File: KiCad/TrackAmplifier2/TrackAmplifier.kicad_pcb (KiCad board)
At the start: 2 copper layers, 105 x 70 mm, 109 parts, among them J1 DB15_Male_MountingHoles, J2 Conn_01x06, Q1 2N7002, U1 ST485EBDR, U10 REF3025, U11 LM35-LP, U2 ST485EBDR, U3 LM78M05_TO252, U4 LMD18200, U5 ST485EBDR, U6 ST485EBDR, U7 INA326, U8 INA326, U9 PIC16F18854-SO

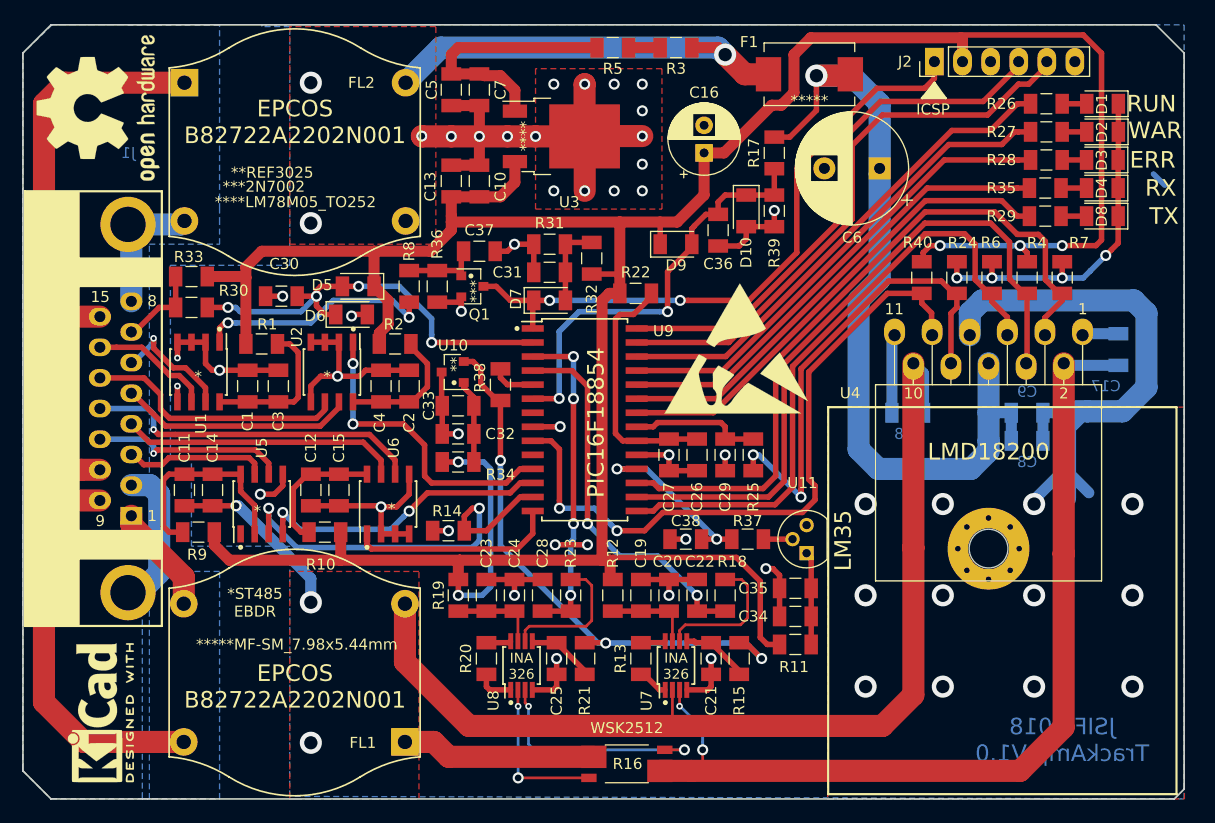
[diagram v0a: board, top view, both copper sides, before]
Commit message: updated schematic and layout, not finished yet. To do: - Update components with real used values
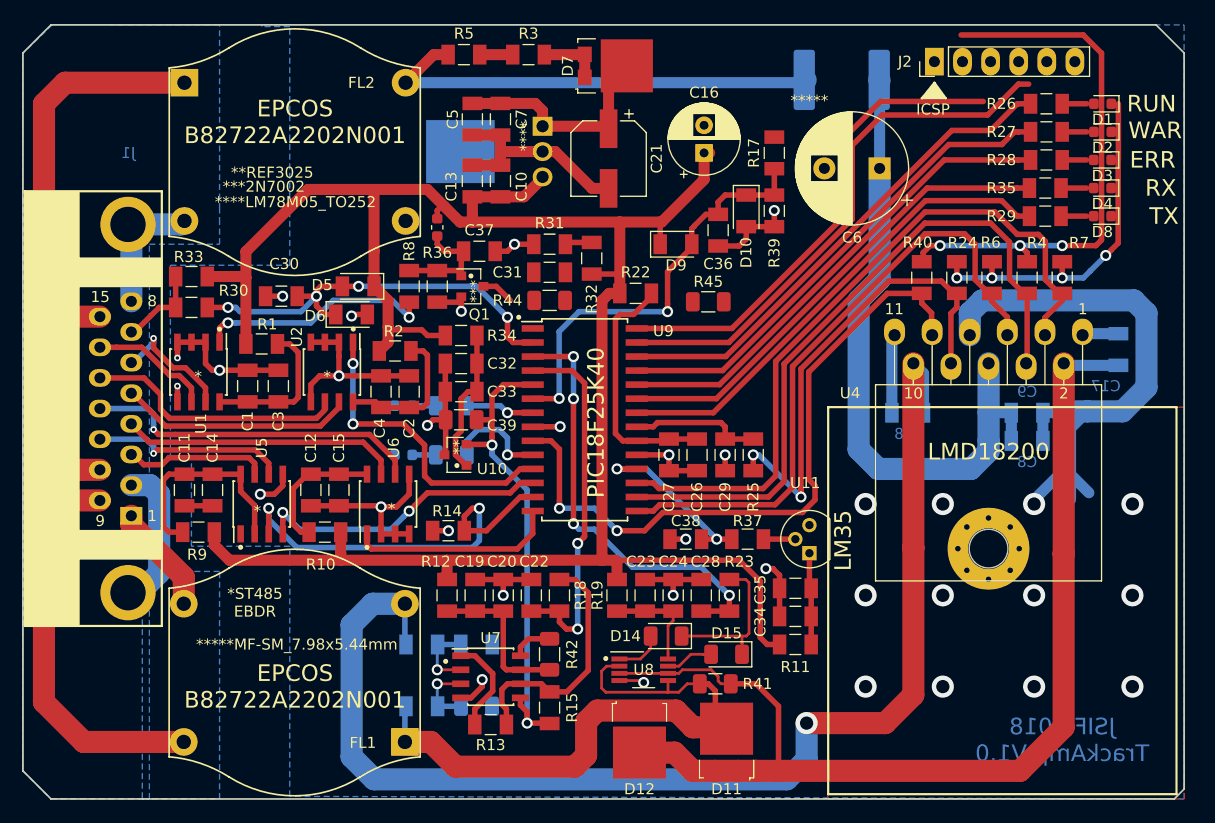
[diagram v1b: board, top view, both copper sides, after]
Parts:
- removed C25: 100n, Capacitor_SMD:C_1206_3216Metric
- removed REF**: ESD-Logo_13.2x12mm_SilkScreen, Symbol:ESD-Logo_13.2x12mm_SilkScreen
- removed REF**: KiCad-Logo2_6mm_SilkScreen, Symbol:KiCad-Logo2_6mm_SilkScreen
- removed REF**: OSHW-Logo2_14.6x12mm_SilkScreen, Symbol:OSHW-Logo2_14.6x12mm_SilkScreen
- added C39: 4.7u, Capacitor_SMD:C_1206_3216Metric, F.Cu at (89.6, 85.7)
- added D11: VS-6ESH06-M3, Package_TO_SOT_SMD:TO-277A, F.Cu at (113.6, 114.7)
- added D12: VS-6ESH06-M3, Package_TO_SOT_SMD:TO-277A, F.Cu at (105.8, 114.8)
- added D13: LED BL ?, LED_SMD:LED_0603_1608Metric, B.Cu at (84.4, 88.9)
- added D14: 1n4148, Diode_SMD:D_1206_3216Metric, F.Cu at (108.2, 105.3)
- added D15: 1n4148, Diode_SMD:D_1206_3216Metric, F.Cu at (113.6, 106.9)
- added D16: LED BL, LED_SMD:LED_0603_1608Metric, B.Cu at (84.4, 84.4)
- added R41: 47E, Resistor_SMD:R_1206_3216Metric, F.Cu at (112.6, 109.6)
- added R42: 4k7, Resistor_SMD:R_1206_3216Metric, F.Cu at (97.6, 106.9)
- added R43: 300E, Resistor_SMD:R_1206_3216Metric, B.Cu at (88.7, 88.9)
- added R44: 470, Resistor_SMD:R_1206_3216Metric, F.Cu at (97.6, 74.9)
- added R45: 470, Resistor_SMD:R_1206_3216Metric, F.Cu at (112.0, 75.0)
- added R46: 300E, Resistor_SMD:R_1206_3216Metric, B.Cu at (88.7, 84.4)
- added R47: NP, Resistor_SMD:R_0603_1608Metric, F.Cu at (87.5, 68.3)
- C1, C11, C12, C13, C19, C2, C23, C26, C32, C34, C38, C5, C8: value 22u -> 4.7u
- C16: value 100u -> 220u
- C21: value 100n -> 470u; footprint Capacitor_SMD:C_1206_3216Metric -> Capacitor_SMD:CP_Elec_6.3x3
- C22, C28: value 1u -> 100n
- C29: value 22u -> 100n
- C30: value 220n -> 100n
- C36: value 220n -> 4.7u
- D1, D4, D8: value LED -> LED GR; footprint LED_SMD:LED_1206_3216Metric -> LED_SMD:LED_0603_1608Metric
- D2: value LED -> LED YE; footprint LED_SMD:LED_1206_3216Metric -> LED_SMD:LED_0603_1608Metric
- D3: value LED -> LED RD; footprint LED_SMD:LED_1206_3216Metric -> LED_SMD:LED_0603_1608Metric
- D7: value 1n4148 -> VS-6ESH06-M3; footprint Diode_SMD:D_1206_3216Metric -> Package_TO_SOT_SMD:TO-277A
- F1: value 3.0A -> 2.5A; footprint Fuse:Fuse_Bourns_MF-SM_7.98x5.44mm -> Fuse:Fuse_2920_7451Metric; moved to B.Cu
- Q1: value 2N7002 -> NTR5103NT1G
- R1, R10, R11, R2, R22, R9: value 10E -> 0E
- R13: value 10E -> 1k
- R14: value 4K7 -> 1k
- R15: value 10E -> 110k
- R16: value 0.025 -> 1k; footprint Resistor_SMD:R_Shunt_2512_6332Metric_0.005-0.2 -> Resistor_SMD:R_1206_3216Metric; moved to B.Cu
- R17: value 10k -> 5k1
- R20, R21: value 10E -> 9k10; moved to B.Cu
- R25: value 1K -> 4k7
- R26, R27, R28, R29, R35: value 330E -> 300E
- R30: value 10k -> 1k
- R31: value 100K -> 110k
- R33: value 1K -> 470
- R38: value 10E -> 1k; moved to B.Cu
- R39: value 50k -> 910R
- R4, R6, R7: value 4K7 -> 4k7
- R8: value 100E -> 1k
- U10: value REF3025 -> MCP1525
- U11: value LM35-LP -> MCP9701A-E/TO
- U3: value LM78M05_TO252 -> L78M05CDT-1-TO-251-3; footprint Package_TO_SOT_SMD:TO-252-2 -> Package_TO_SOT_THT:TO-251-3-1EP_Horizontal_TabDown; moved to B.Cu
- U7: value INA326 -> MCP6N11; footprint Package_SO:MSOP-8_3x3mm_P0.65mm -> Package_SO:SOIC-8_3.9x4.9mm_P1.27mm
- U8: value INA326 -> INA2180; footprint Package_SO:MSOP-8_3x3mm_P0.65mm -> Package_SO:VSSOP-8_3.0x3.0mm_P0.65mm
- U9: value PIC16F18854-SO -> PIC18F25K40
- moved C21 46.2 mm to (103.0, 62.1), turned to 270 degrees
- moved R38 23.6 mm to (91.0, 106.0), turned to 0 degrees
- moved D7 22.0 mm to (103.6, 53.7), turned to 90 degrees
- moved R15 17.7 mm to (97.6, 111.7)
- moved U7 16.8 mm to (92.3, 109.0), turned to 0 degrees
- moved C20 15.0 mm to (93.4, 101.6)
- moved R12 15.0 mm to (88.4, 101.6)
- moved R18 15.0 mm to (98.5, 101.6)
- moved C19 15.0 mm to (90.9, 101.6)
- moved C22 15.0 mm to (96.0, 101.6)
- moved R13 14.8 mm to (92.3, 113.3), turned to 180 degrees
- moved R21 14.8 mm to (86.1, 106.0), turned to 0 degrees
- moved R16 14.6 mm to (91.0, 111.6), turned to 0 degrees
- moved C23 14.4 mm to (106.3, 101.6)
- moved C24 14.4 mm to (108.8, 101.6)
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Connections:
- C17 pad 2: PWM1 -> OCC1
- C21 pad 1: GND -> Net-(C21-Pad1)
- C21 pad 2: Net-(C21-Pad2) -> GND
- C5 pad 2: +15V -> Net-(C21-Pad1)
- C7 pad 2: +15V -> Net-(C21-Pad1)
- D7 pad 1: RST -> Net-(D7-Pad1)
- D7 pad 2: Net-(C31-Pad2) -> Net-(D7-Pad1)
- FL1 pad 1: Net-(FL1-Pad1) -> OCC2
- J2 pad 1: RST -> VPP
- R15 pad 1: VREF -> Net-(R13-Pad1)
- R15 pad 2: Net-(C21-Pad2) -> VREF
- R16 pad 1: PWM1 -> Net-(R16-Pad1)
- R16 pad 2: OCC1 -> GND
- R18 pad 2: Net-(R18-Pad2) -> Net-(R13-Pad1)
- R20 pad 1: Net-(R20-Pad1) -> Net-(R16-Pad1)
- R20 pad 2: Net-(R20-Pad2) -> OCC2
- R21 pad 1: VREF -> PWM2
- R21 pad 2: Net-(C25-Pad2) -> Net-(R21-Pad2)
- R23 pad 2: Net-(R23-Pad2) -> Net-(D14-Pad1)
- R3 pad 1: Vbus_flt -> Net-(R3-Pad1)
- R3 pad 2: Net-(R3-Pad2) -> Net-(D7-Pad1)
- R38 pad 1: VREF -> Net-(R21-Pad2)
- R38 pad 2: Net-(R38-Pad2) -> GND
- R5 pad 1: Net-(R3-Pad2) -> Vbus_flt
- R5 pad 2: +15V -> Net-(R3-Pad1)
- U3 pad 1: +15V -> Net-(C21-Pad1)
- U4 pad 2: PWM1 -> OCC1
- U7 pad 1: Net-(R13-Pad1) -> Net-(R13-Pad2)
- U7 pad 2: PWM2 -> Net-(R21-Pad2)
- U7 pad 3: PWM1 -> Net-(R16-Pad1)
- U7 pad 5: Net-(C21-Pad2) -> VREF
- U7 pad 6: Net-(R18-Pad2) -> Net-(R13-Pad1)
- U7 pad 8: Net-(R13-Pad2) -> Net-(R42-Pad2)
- U8 pad 1: Net-(R20-Pad1) -> Net-(D14-Pad2)
- U8 pad 5: Net-(C25-Pad2) -> OCC2
- U8 pad 6: Net-(R23-Pad2) -> OCC1
- U8 pad 7: Net-(C23-Pad2) -> Net-(D15-Pad2)
- U8 pad 8: Net-(R20-Pad2) -> Net-(C23-Pad2)
- U9 pad 5: Net-(R38-Pad2) -> VREF
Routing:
- net PWM1: track 85.3 -> 0.00 mm, vias 2 -> 0
- net OCC1: track 21.1 -> 100.5 mm, vias 2 -> 0
- net RST: track 58.2 -> 2.96 mm, vias 2 -> 0
- net GND: track 270.0 -> 226.7 mm, vias 61 -> 38
- net OCC2: track 14.3 -> 57.6 mm, vias 2 -> 0
- net +5V: track 283.0 -> 244.8 mm, vias 5 -> 3
- net +15V: track 23.4 -> 0.00 mm
- net Net-(C21-Pad1): track 0.00 -> 20.5 mm
- net PWM2: track 92.9 -> 112.9 mm, vias 0 -> 1
- net Net-(R13-Pad1): track 2.76 -> 22.6 mm
- net Net-(FL1-Pad1): track 17.6 -> 0.00 mm
- net Net-(C6-Pad1): track 77.4 -> 61.3 mm, vias 1 -> 0
- net Net-(D14-Pad1): track 0.00 -> 14.3 mm
- net Net-(R18-Pad2): track 12.8 -> 0.00 mm
- net Net-(R23-Pad2): track 12.7 -> 0.00 mm
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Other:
- board text added: "PIC18F25K40"
- board text removed: "INA 326"
- board text removed: "PIC16F18854"
- board text removed: "WSK2512"

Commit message: Updated schematic according to proto board.
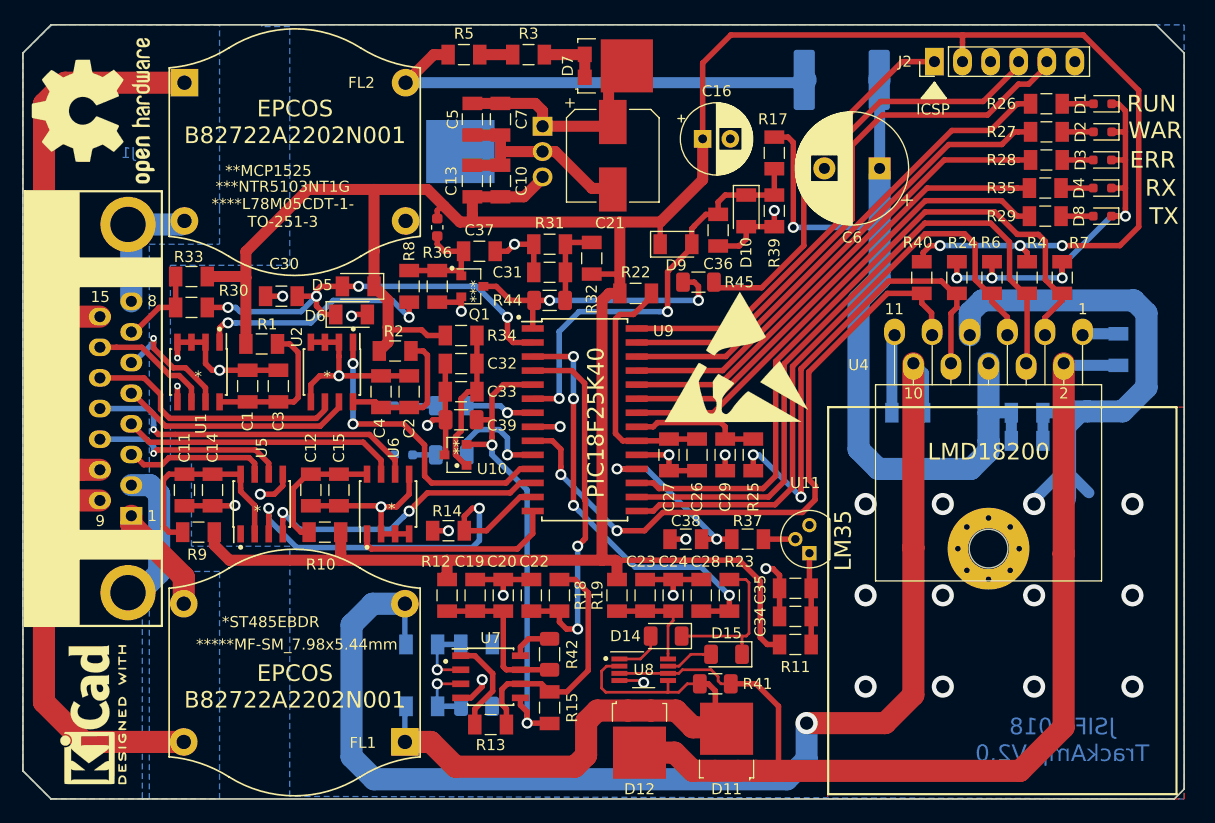
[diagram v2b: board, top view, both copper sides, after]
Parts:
- added REF**: ESD-Logo_13.2x12mm_SilkScreen, Symbol:ESD-Logo_13.2x12mm_SilkScreen, F.Cu at (114.5, 80.0)
- added REF**: OSHW-Logo2_14.6x12mm_SilkScreen, Symbol:OSHW-Logo2_14.6x12mm_SilkScreen, F.Cu at (56.4, 57.8)
- added REF**: KiCad-Logo2_6mm_SilkScreen, Symbol:KiCad-Logo2_6mm_SilkScreen, F.Cu at (56.4, 112.4)
- C21: footprint Capacitor_SMD:CP_Elec_6.3x3 -> Capacitor_SMD:CP_Elec_8x10.5
- D1, D13, D16, D2, D3, D4, D8: footprint LED_SMD:LED_0603_1608Metric -> Diode_SMD:LED_0.8x0.8
- moved R45 1.99 mm to (111.1, 73.3)
- moved C16 1.28 mm to (111.5, 60.3), turned to 0 degrees
- moved C21 0.46 mm to (103.3, 61.8)
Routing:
- net +5V: track 244.8 -> 283.2 mm
- net VPP: track 0.00 -> 32.9 mm
- net RST: track 2.96 -> 25.4 mm, vias 0 -> 2
- net Net-(C6-Pad1): track 61.3 -> 78.7 mm, vias 0 -> 1
- net GND: track 226.7 -> 237.0 mm, vias 38 -> 39
- net Net-(C31-Pad2): track 2.45 -> 7.54 mm
- net ICSPDAT: track 44.0 -> 48.9 mm
- net ICSPCLK: track 49.0 -> 51.7 mm
- net THFLG: track 62.3 -> 60.5 mm
- net OCC: track 39.5 -> 38.6 mm
- net Net-(D2-Pad2): track 2.22 -> 2.83 mm
- net Net-(D1-Pad2): track 2.22 -> 2.83 mm
- net Net-(D8-Pad2): track 2.30 -> 2.91 mm
- net Net-(D4-Pad2): track 2.30 -> 2.91 mm
- net Net-(D3-Pad2): track 2.20 -> 2.81 mm
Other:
- board text added: "****L78M05CDT-1- TO-251-3"
- board text added: "***NTR5103NT1G"
- board text added: "**MCP1525"
- board text added: "*ST485EBDR"
- board text added: "JSIF 2018 TrackAmp V2.0"
- board text added: "OCCUPIED"
- board text removed: "****LM78M05_TO252"
- board text removed: "***2N7002"
- board text removed: "**REF3025"
- board text removed: "*ST485 EBDR"
- board text removed: "C17"
- board text removed: "C18"
- board text removed: "C8"
- board text removed: "C9"
- board text removed: "JSIF 2018 TrackAmp V1.0"

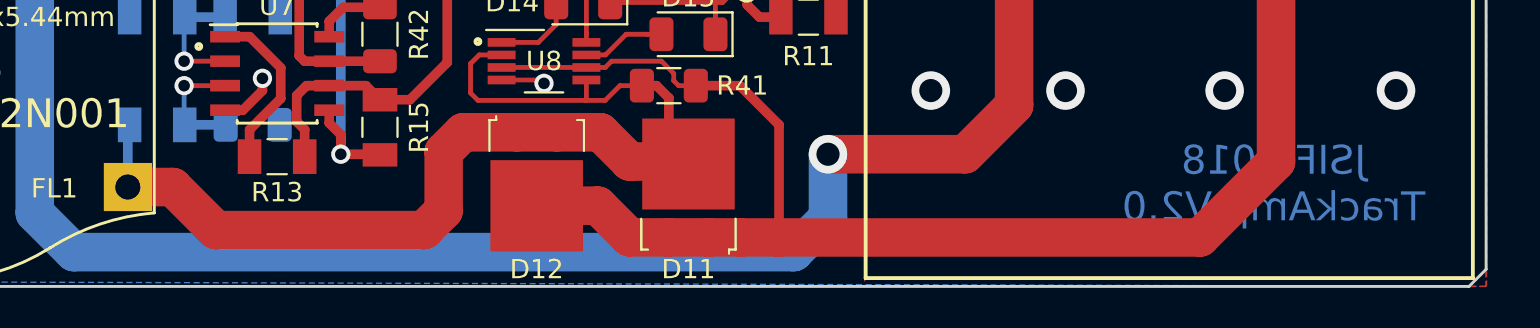
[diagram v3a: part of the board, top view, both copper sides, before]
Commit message: updated year notifications to 2019
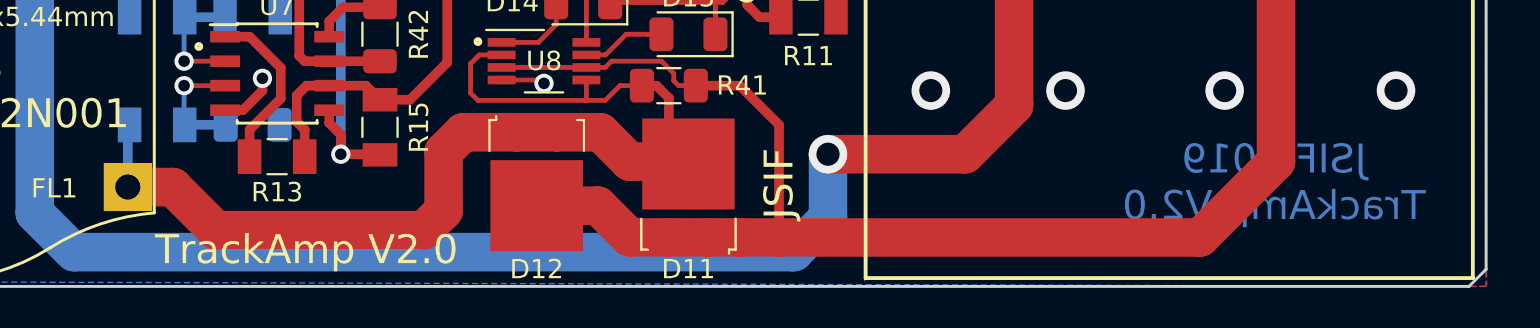
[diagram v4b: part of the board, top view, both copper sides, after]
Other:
- board text added: "JSIF"
- board text added: "JSIF 2019 TrackAmp V2.0"
- board text added: "TrackAmp V2.0"
- board text removed: "JSIF 2018 TrackAmp V2.0"
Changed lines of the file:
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@@
   (general
     (thickness 1.6)
-    (drawings 85)
+    (drawings 87)
     (tracks 918)
     (zones 0)
@@
     )
   )
+  (gr_text JSIF (at 118.326 114.666 90) (layer F.SilkS)
+    (effects (font (size 1.5 1.5) (thickness 0.3)))
+  )
+  (gr_text "TrackAmp V2.0" (at 93.815 118.095) (layer F.SilkS)
+    (effects (font (size 1.5 1.5) (thickness 0.3)))
+  )
   (gr_text 8 (at 61.684 74.9785) (layer B.SilkS)
     (effects (font (size 1 1) (thickness 0.15)) (justify mirror))
@@
     (effects (font (size 1.5 1.5) (thickness 0.3)) (justify mirror))
   )
-  (gr_text "JSIF 2018 \nTrackAmp V2.0" (at 143.98 114.666) (layer B.SilkS)
+  (gr_text "JSIF 2019 \nTrackAmp V2.0" (at 144 114.6) (layer B.SilkS)
     (effects (font (size 1.5 1.5) (thickness 0.3)) (justify mirror))
   )
@@
   (gr_line (start 132.423 55.357) (end 131.534 56.5) (layer F.SilkS) (width 0.2))
   (gr_line (start 133.185 56.5) (end 132.423 55.357) (layer F.SilkS) (width 0.2))
-  (gr_text "JSIF 2018 \nTrackAmp V2.0" (at 143.98 114.666) (layer B.Cu)
+  (gr_text "JSIF 2019 \nTrackAmp V2.0" (at 144 114.6) (layer B.Cu)
     (effects (font (size 1.5 1.5) (thickness 0.3)) (justify mirror))
   )

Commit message: some minor changes
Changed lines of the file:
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@@
   (general
     (thickness 1.6)
-    (drawings 87)
+    (drawings 103)
     (tracks 918)
     (zones 0)
@@
     (tags SOT-23)
     (attr smd)
-    (fp_text reference U10 (at -3.302 -1.27 180) (layer F.SilkS)
+    (fp_text reference U10 (at 0 -2.3622 180) (layer F.SilkS)
       (effects (font (size 1 1) (thickness 0.15)))
     )
@@
     )
   )
-  (gr_text JSIF (at 118.326 114.666 90) (layer F.SilkS)
+  (gr_line (start 132.446102 56.09166) (end 132.573102 56.21866) (layer B.SilkS) (width 0.2))
+  (gr_line (start 132.573102 56.21866) (end 132.446102 56.21866) (layer B.SilkS) (width 0.2))
+  (gr_line (start 132.446102 55.32966) (end 131.430102 56.72666) (layer B.SilkS) (width 0.2))
+  (gr_line (start 133.462102 56.59966) (end 132.446102 55.32966) (layer B.SilkS) (width 0.2))
+  (gr_line (start 133.589102 56.72666) (end 133.462102 56.59966) (layer B.SilkS) (width 0.2))
+  (gr_line (start 131.430102 56.72666) (end 133.589102 56.72666) (layer B.SilkS) (width 0.2))
+  (gr_text ICSP (at 132.319102 57.74266 180) (layer B.SilkS)
+    (effects (font (size 1 1) (thickness 0.15)) (justify mirror))
+  )
+  (gr_line (start 131.684102 56.59966) (end 132.446102 55.45666) (layer B.SilkS) (width 0.2))
+  (gr_line (start 132.446102 55.45666) (end 133.335102 56.59966) (layer B.SilkS) (width 0.2))
+  (gr_line (start 133.335102 56.59966) (end 131.684102 56.59966) (layer B.SilkS) (width 0.2))
+  (gr_line (start 131.823802 56.52346) (end 132.446102 55.71066) (layer B.SilkS) (width 0.2))
+  (gr_line (start 132.446102 55.71066) (end 133.081102 56.47266) (layer B.SilkS) (width 0.2))
+  (gr_line (start 132.954102 56.47266) (end 132.065102 56.47266) (layer B.SilkS) (width 0.2))
+  (gr_line (start 132.192102 56.34566) (end 132.446102 55.96466) (layer B.SilkS) (width 0.2))
+  (gr_line (start 132.573102 56.09166) (end 132.827102 56.34566) (layer B.SilkS) (width 0.2))
+  (gr_line (start 132.700102 56.34566) (end 132.319102 56.34566) (layer B.SilkS) (width 0.2))
+  (gr_text JSIF (at 119.596 118.222) (layer F.SilkS)
     (effects (font (size 1.5 1.5) (thickness 0.3)))
   )
@@
     (effects (font (size 1.5 1.5) (thickness 0.3)) (justify mirror))
   )
-  (gr_text ICSP (at 132.296 57.643) (layer F.SilkS)
+  (gr_text ICSP (at 132.55 57.643) (layer F.SilkS)
     (effects (font (size 1 1) (thickness 0.15)))
   )
@@
     (effects (font (size 1 1) (thickness 0.15)))
   )
-  (gr_circle (center 88.8 72) (end 88.8762 72.1016) (layer F.SilkS) (width 0.2))
-  (gr_circle (center 89.243 89.8502) (end 89.3192 89.9518) (layer F.SilkS) (width 0.2))
+  (gr_circle (center 88.7604 72.6798) (end 88.8366 72.7814) (layer F.SilkS) (width 0.2))
+  (gr_circle (center 91.0972 89.8756) (end 91.1734 89.9772) (layer F.SilkS) (width 0.2))
   (gr_text *ST485EBDR (at 72.4 104) (layer F.SilkS)
     (effects (font (size 1 1) (thickness 0.15)))
@@
   (gr_circle (center 67.78 77.5058) (end 67.8562 77.6074) (layer F.SilkS) (width 0.2))
   (gr_circle (center 79.8704 77.5058) (end 79.9466 77.6074) (layer F.SilkS) (width 0.2))
-  (gr_circle (center 94.831 76.439) (end 94.9072 76.5406) (layer F.SilkS) (width 0.2))
+  (gr_circle (center 94.6786 77.455) (end 94.7548 77.5566) (layer F.SilkS) (width 0.2))
   (gr_circle (center 102.705 107.3) (end 102.7812 107.4016) (layer F.SilkS) (width 0.2))
-  (gr_circle (center 88.227 107.554) (end 88.3032 107.6556) (layer F.SilkS) (width 0.2))
+  (gr_circle (center 88.227 107.046) (end 88.3032 107.1476) (layer F.SilkS) (width 0.2))
   (gr_text LM35 (at 124.168 96.632 90) (layer F.SilkS)
     (effects (font (size 1.5 1.5) (thickness 0.3)))
